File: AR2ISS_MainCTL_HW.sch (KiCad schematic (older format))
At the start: 3 parts

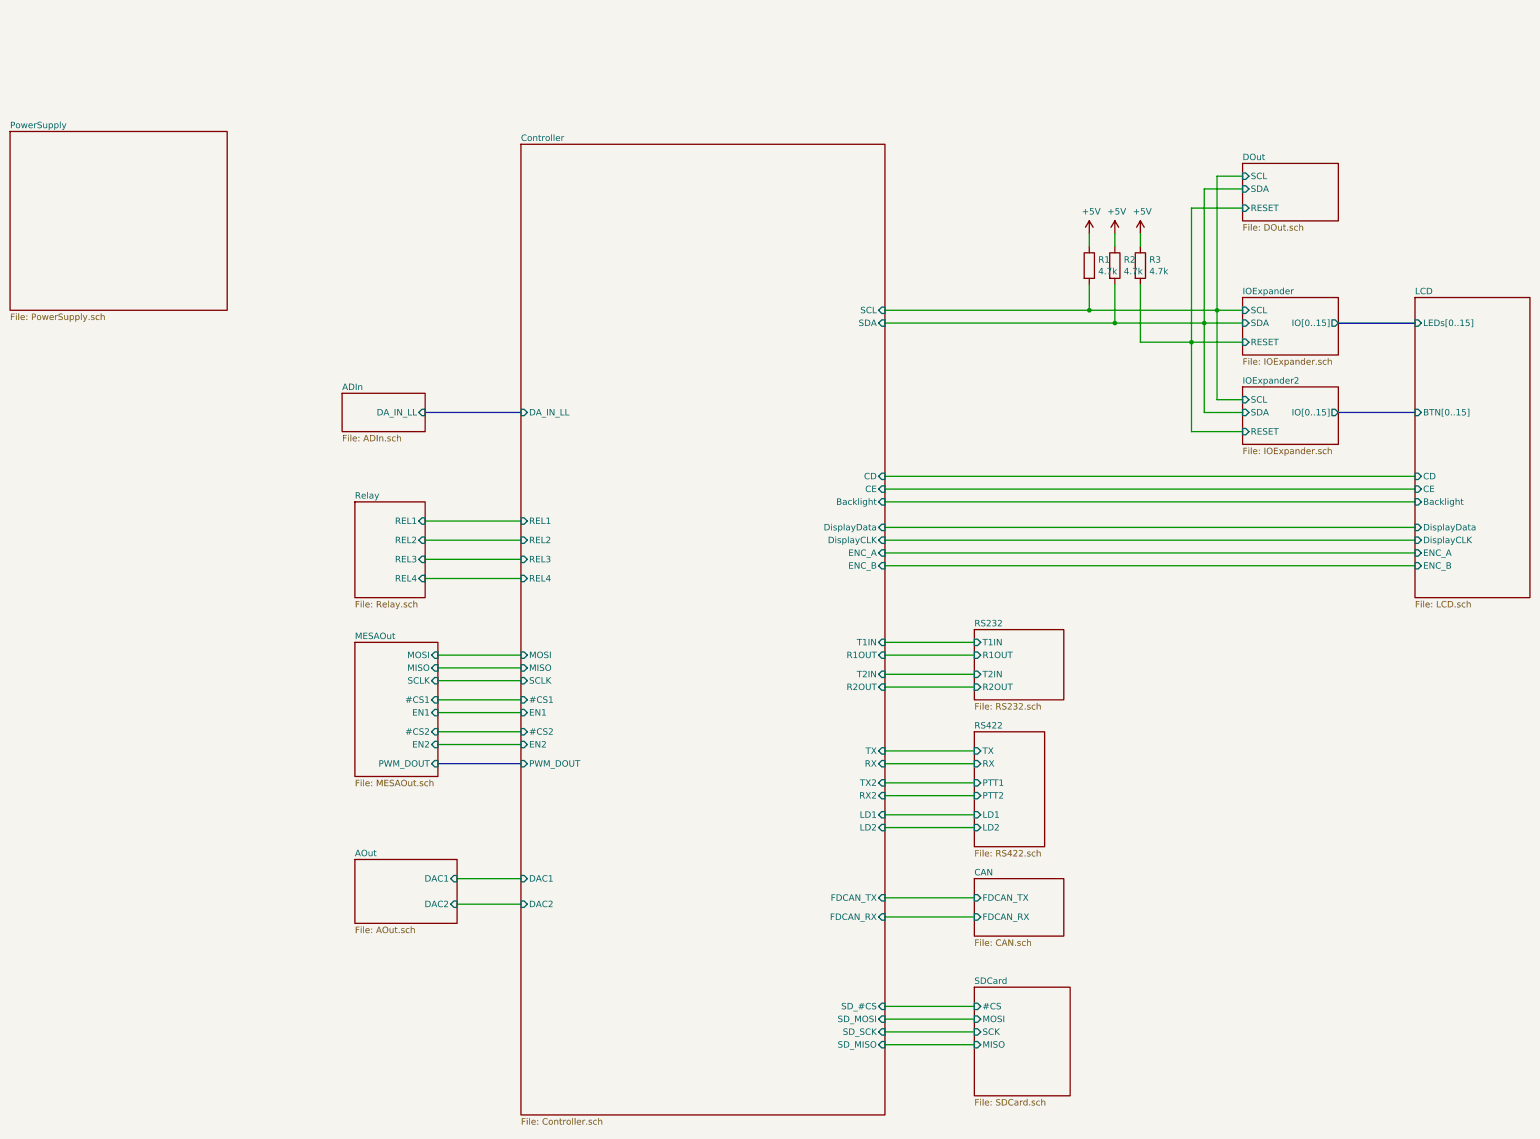
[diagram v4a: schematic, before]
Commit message: add TLE5602
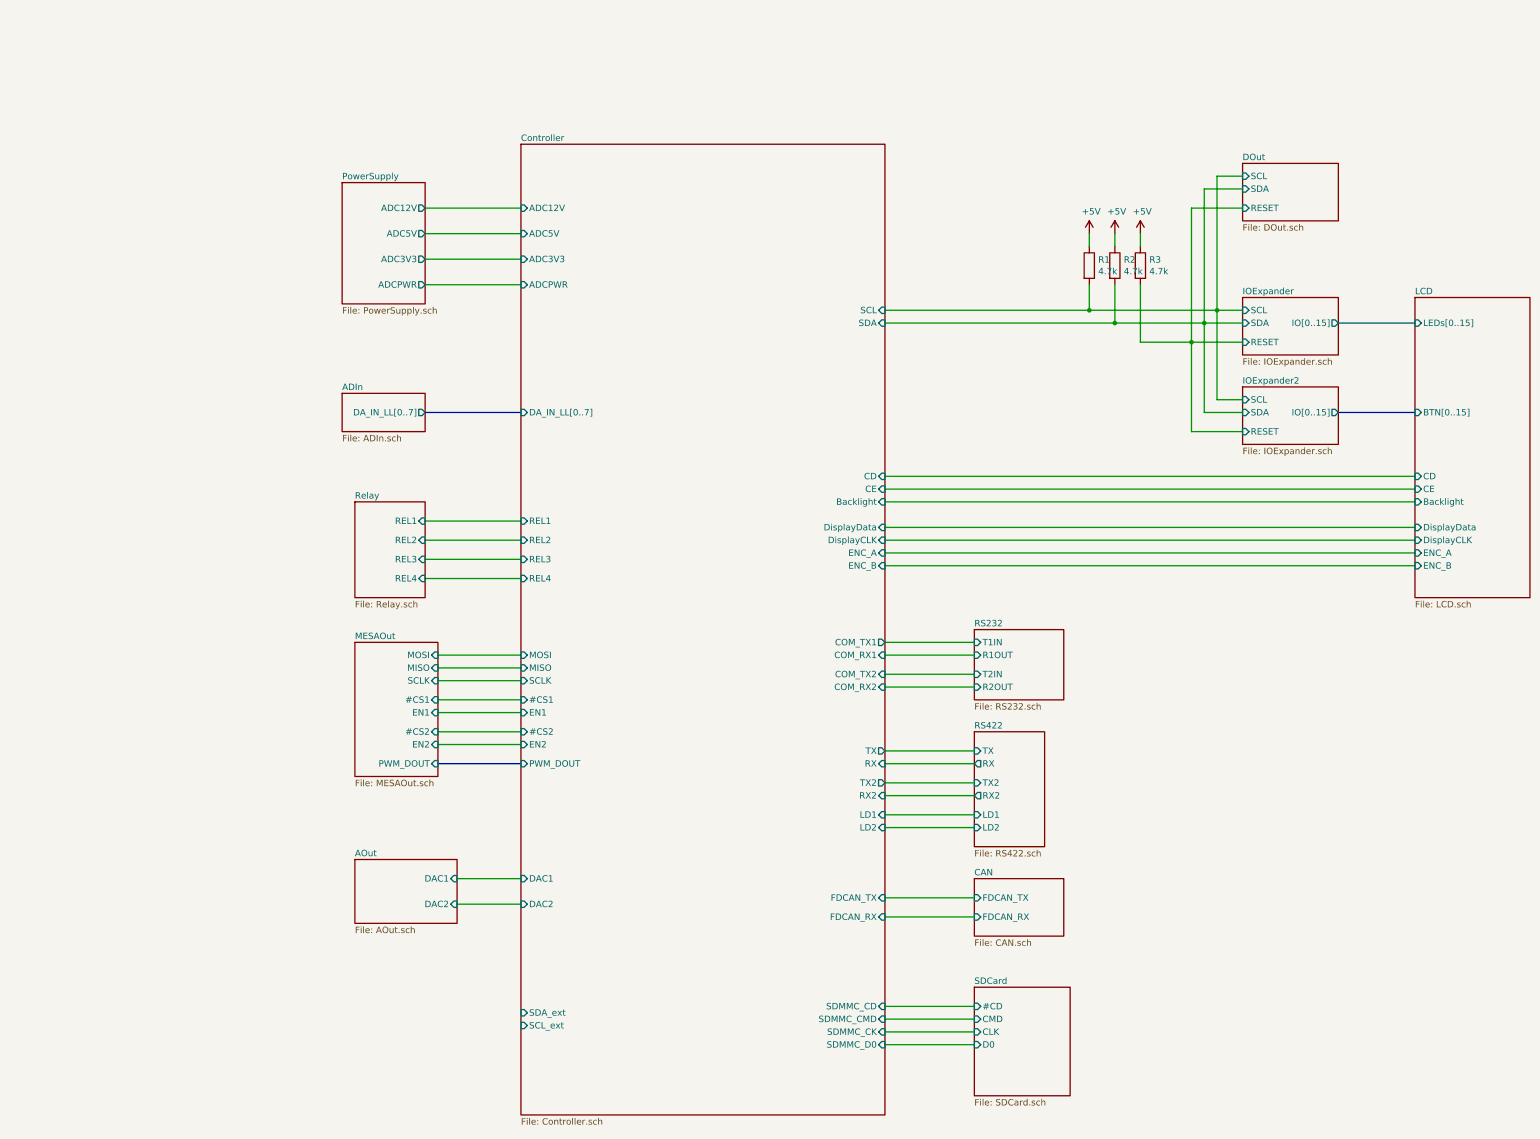
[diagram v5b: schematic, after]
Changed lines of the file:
@@
-$EndSheet
-$Sheet
-S 4900 4350 650  300
-U 6069F05D
-F0 "ADIn" 50
-F1 "ADIn.sch" 50
-F2 "DA_IN_LL" I R 5550 4500 50
 $EndSheet
 $Sheet
@@
 	11150 3200 11150 3100
 $Sheet
-S 2300 2300 1700 1400
+S 4900 2700 650  950
 U 60A2EE09
 F0 "PowerSupply" 50
 F1 "PowerSupply.sch" 50
+F2 "ADC12V" O R 5550 2900 50
+F3 "ADCPWR" O R 5550 3500 50
+F4 "ADC5V" O R 5550 3100 50
+F5 "ADC3V3" O R 5550 3300 50
 $EndSheet
 $Sheet
@@
 Wire Wire Line
 	13300 5000 9150 5000
-$Sheet
-S 6300 2400 2850 7600
-U 60AEFCAF
-F0 "Controller" 50
-F1 "Controller.sch" 50
-F2 "R2OUT" I R 9150 6650 50
-F3 "T2IN" I R 9150 6550 50
-F4 "R1OUT" I R 9150 6400 50
-F5 "T1IN" I R 9150 6300 50
-F6 "FDCAN_TX" I R 9150 8300 50
-F7 "FDCAN_RX" I R 9150 8450 50
-F8 "TX" I R 9150 7150 50
-F9 "RX" I R 9150 7250 50
-F10 "TX2" I R 9150 7400 50
-F11 "RX2" I R 9150 7500 50
-F12 "LD1" I R 9150 7650 50
-F13 "LD2" I R 9150 7750 50
-F14 "SDA" I R 9150 3800 50
-F15 "SCL" I R 9150 3700 50
-F16 "CD" I R 9150 5000 50
-F17 "CE" I R 9150 5100 50
-F18 "Backlight" I R 9150 5200 50
-F19 "DisplayData" I R 9150 5400 50
-F20 "DisplayCLK" I R 9150 5500 50
-F21 "ENC_A" I R 9150 5600 50
-F22 "ENC_B" I R 9150 5700 50
-F23 "REL1" I L 6300 5350 50
-F24 "REL2" I L 6300 5500 50
-F25 "REL3" I L 6300 5650 50
-F26 "REL4" I L 6300 5800 50
-F27 "DA_IN_LL" I L 6300 4500 50
-F28 "DAC1" I L 6300 8150 50
-F29 "DAC2" I L 6300 8350 50
-F30 "MOSI" I L 6300 6400 50
-F31 "MISO" I L 6300 6500 50
-F32 "SCLK" I L 6300 6600 50
-F33 "#CS1" I L 6300 6750 50
-F34 "#CS2" I L 6300 7000 50
-F35 "EN1" I L 6300 6850 50
-F36 "EN2" I L 6300 7100 50
-F37 "PWM_DOUT" I L 6300 7250 50
-F38 "SD_#CS" I R 9150 9150 50
-F39 "SD_MOSI" I R 9150 9250 50
-F40 "SD_MISO" I R 9150 9450 50
-F41 "SD_SCK" I R 9150 9350 50
-$EndSheet
-Wire Bus Line
-	5550 4500 6300 4500
 Wire Wire Line
 	5550 5350 6300 5350
@@
 F0 "SDCard" 50
 F1 "SDCard.sch" 50
-F2 "#CS" I L 9850 9150 50
-F3 "MOSI" I L 9850 9250 50
-F4 "SCK" I L 9850 9350 50
-F5 "MISO" I L 9850 9450 50
+F2 "#CD" I L 9850 9150 50
+F3 "CMD" I L 9850 9250 50
+F4 "CLK" I L 9850 9350 50
+F5 "D0" I L 9850 9450 50
 $EndSheet
 $Sheet
@@
 F3 "LD2" I L 9850 7750 50
 F4 "TX" I L 9850 7150 50
-F5 "PTT2" I L 9850 7500 50
-F6 "PTT1" I L 9850 7400 50
-F7 "RX" I L 9850 7250 50
+F5 "TX2" I L 9850 7400 50
+F6 "RX" O L 9850 7250 50
+F7 "RX2" O L 9850 7500 50
+$EndSheet
+Wire Bus Line
+	5550 4500 6300 4500
+$Sheet
+S 4900 4350 650  300
+U 6069F05D
+F0 "ADIn" 50
+F1 "ADIn.sch" 50
+F2 "DA_IN_LL[0..7]" O R 5550 4500 50
+$EndSheet
+Wire Wire Line
+	6300 2900 5550 2900
+Wire Wire Line
+	5550 3100 6300 3100
+Wire Wire Line
+	6300 3300 5550 3300
+Wire Wire Line
+	5550 3500 6300 3500
+$Sheet
+S 6300 2400 2850 7600
+U 60AEFCAF
+F0 "Controller" 50
+F1 "Controller.sch" 50
+F2 "FDCAN_TX" I R 9150 8300 50
+F3 "FDCAN_RX" I R 9150 8450 50
+F4 "LD1" I R 9150 7650 50
+F5 "LD2" I R 9150 7750 50
+F6 "SDA" I R 9150 3800 50
+F7 "SCL" I R 9150 3700 50
+F8 "CD" I R 9150 5000 50
+F9 "CE" I R 9150 5100 50
+F10 "Backlight" I R 9150 5200 50
+F11 "DisplayData" I R 9150 5400 50
+F12 "DisplayCLK" I R 9150 5500 50
+F13 "ENC_A" I R 9150 5600 50
+F14 "ENC_B" I R 9150 5700 50
+F15 "REL1" I L 6300 5350 50
+F16 "REL2" I L 6300 5500 50
+F17 "REL3" I L 6300 5650 50
+F18 "REL4" I L 6300 5800 50
+F19 "DAC1" I L 6300 8150 50
+F20 "DAC2" I L 6300 8350 50
+F21 "MOSI" I L 6300 6400 50
+F22 "MISO" I L 6300 6500 50
+F23 "SCLK" I L 6300 6600 50
+F24 "#CS1" I L 6300 6750 50
+F25 "#CS2" I L 6300 7000 50
+F26 "EN1" I L 6300 6850 50
+F27 "EN2" I L 6300 7100 50
+F28 "PWM_DOUT" I L 6300 7250 50
+F29 "DA_IN_LL[0..7]" I L 6300 4500 50
+F30 "ADC12V" I L 6300 2900 50
+F31 "ADC5V" I L 6300 3100 50
+F32 "ADCPWR" I L 6300 3500 50
+F33 "ADC3V3" I L 6300 3300 50
+F34 "TX" O R 9150 7150 50
+F35 "RX" I R 9150 7250 50
+F36 "TX2" O R 9150 7400 50
+F37 "RX2" I R 9150 7500 50
+F38 "SDMMC_CD" I R 9150 9150 50
+F39 "SDMMC_CMD" I R 9150 9250 50
+F40 "SDMMC_CK" I R 9150 9350 50
+F41 "SDMMC_D0" I R 9150 9450 50
+F42 "COM_TX1" O R 9150 6300 50
+F43 "COM_RX1" I R 9150 6400 50
+F44 "COM_TX2" I R 9150 6550 50
+F45 "COM_RX2" I R 9150 6650 50
+F46 "SDA_ext" I L 6300 9200 50
+F47 "SCL_ext" I L 6300 9300 50
 $EndSheet
 $EndSCHEMATC

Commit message: placement, routing
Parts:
- added R100, R102, R78: 0R, Resistor_SMD:R_0603_1608Metric, symbol AR2ISS:R
- added R101, R76, R77, R99: NB, Resistor_SMD:R_0603_1608Metric, symbol AR2ISS:R
- added R75: 4.7k, Resistor_SMD:R_0603_1608Metric, symbol AR2ISS:R
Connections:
- net +5V: now also R101.1, R75.1, R77.1, R99.1
- new net GND: R100.2, R102.2, R76.2, R78.2
- new net IOExpander/A0: R75.2, R76.1
- new net IOExpander/A1: R100.1, R99.2
- new net IOExpander2/A0: R77.2, R78.1
- new net IOExpander2/A1: R101.2, R102.1
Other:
- moved on the sheet: R1, R2, R3
